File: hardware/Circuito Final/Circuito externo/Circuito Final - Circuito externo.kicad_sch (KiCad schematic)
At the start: 43 parts, among them J1 Conn_02x19_Odd_Even, J2 Conn_02x19_Odd_Even, J3 Conn_01x02, J4 Conn_01x02, Q1 FDMS6681Z, Q2 FDMS6681Z, Q3 MMBT2222A, SW1 SW_SPDT, SW2 SW_DIP_x04, SW3 SW_DIP_x04, SW4 SW_DIP_x01, SW5 SW_DIP_x01, SW6 SW_DIP_x01, U1 Opamp_Quad, U2 ICL7660, U3 INA180A1

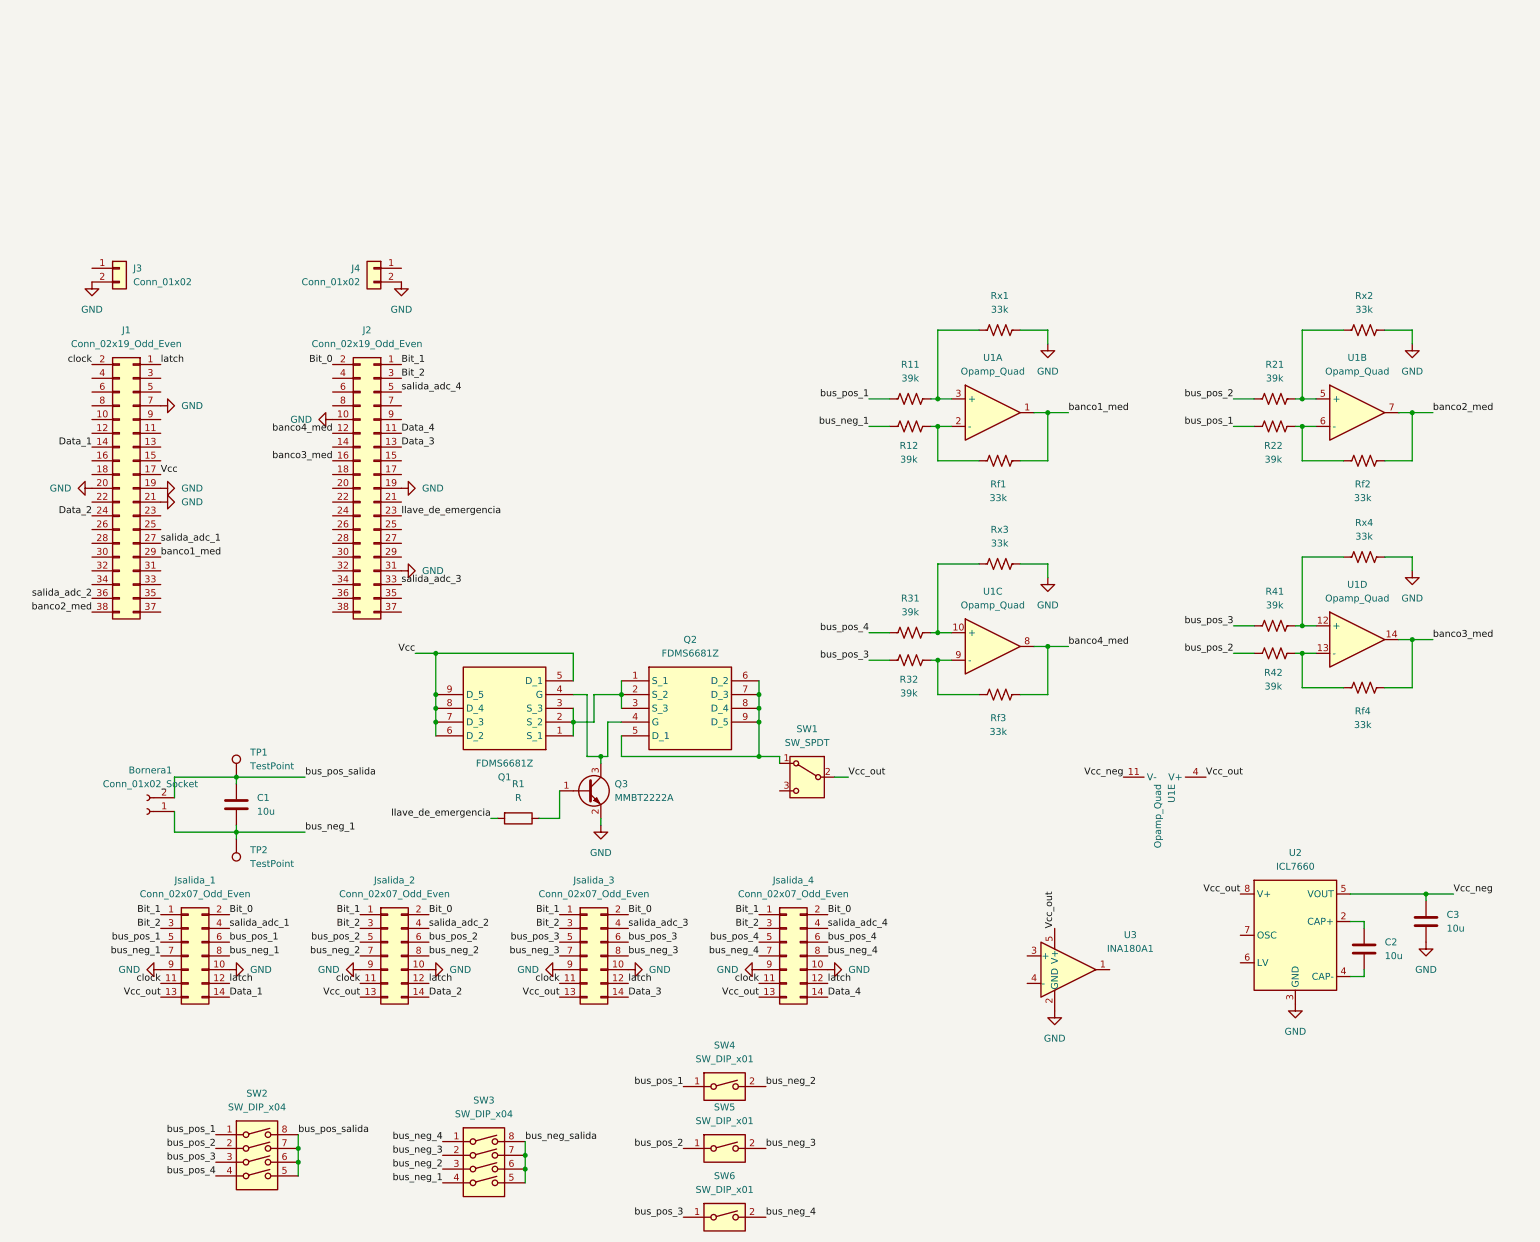
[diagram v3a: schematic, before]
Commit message: clasifica los bloques en el esquematico de kicad
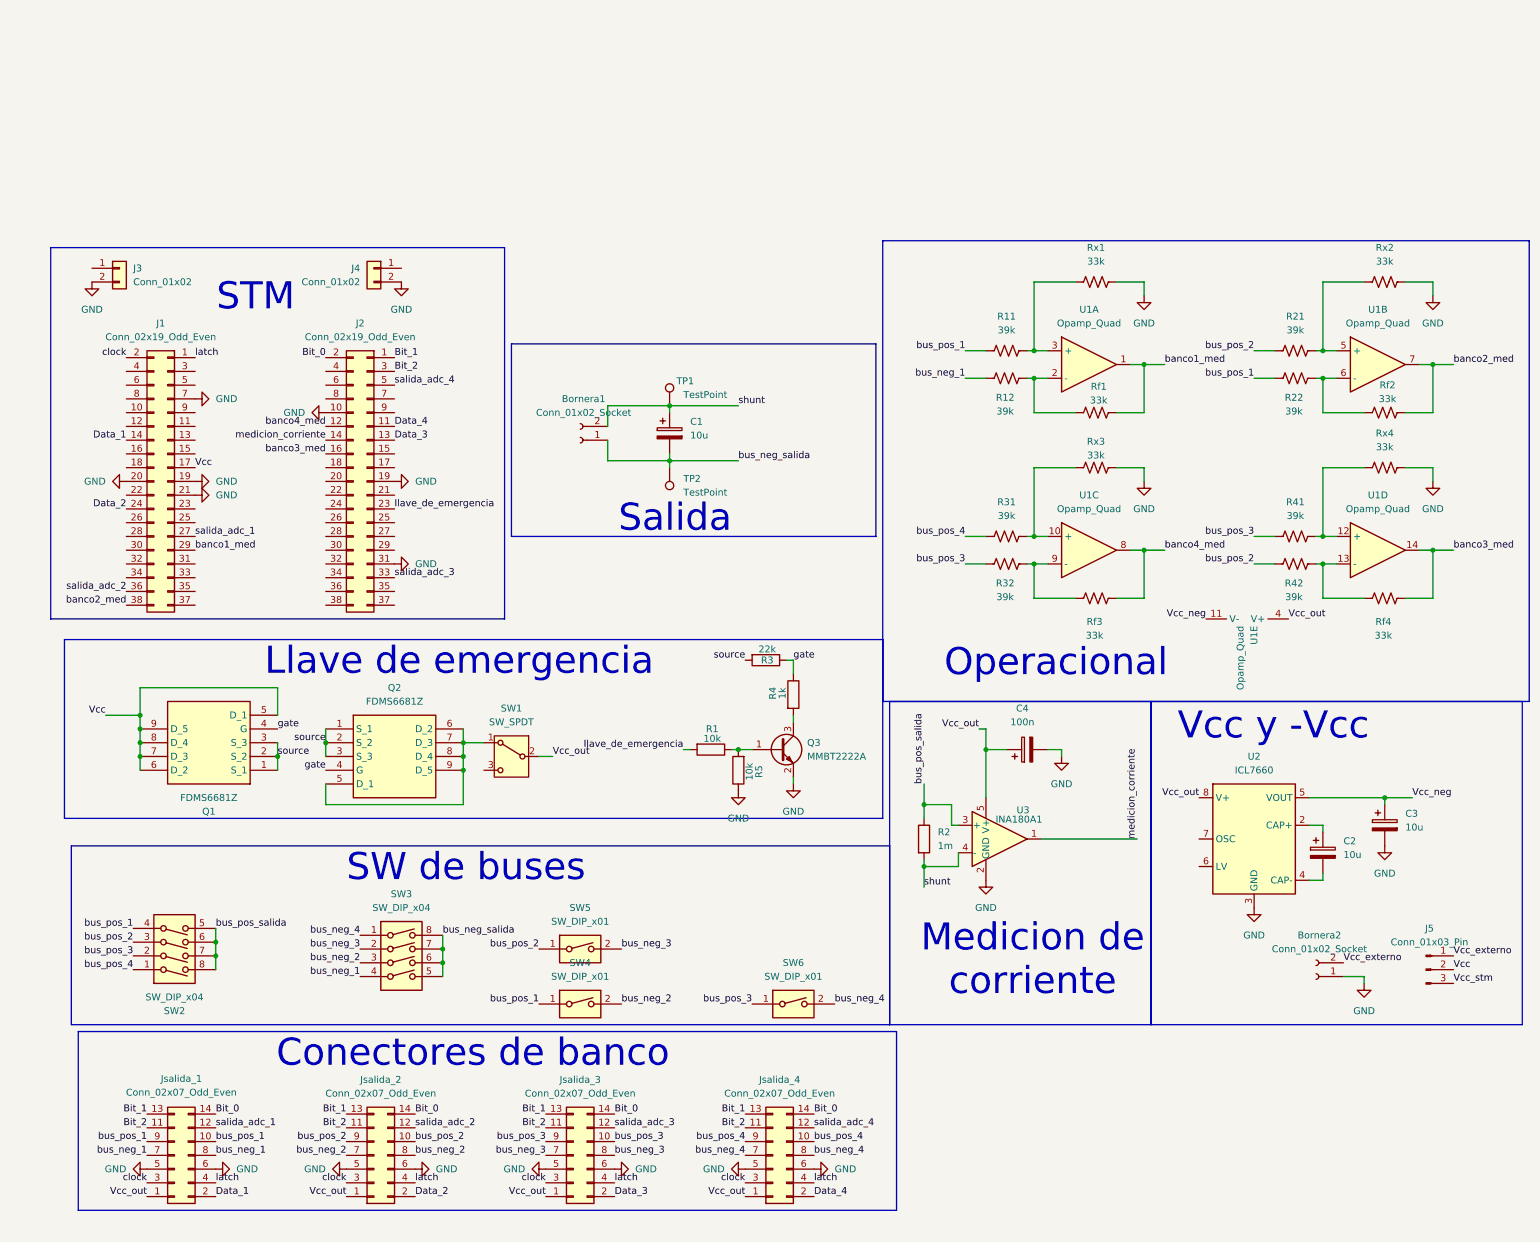
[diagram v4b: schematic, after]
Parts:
- added Bornera2: Conn_01x02_Socket, Huellas:TerminalBlock_bornier-2_P5.08mm, symbol Connector:Conn_01x02_Socket
- added C4: 100n, Capacitor_SMD:C_1206_3216Metric_Pad1.33x1.80mm_HandSolder, symbol Device:C_Polarized
- added J5: Conn_01x03_Pin, symbol Connector:Conn_01x03_Pin
- added R2: 1m, Resistor_SMD:R_2512_6332Metric_Pad1.40x3.35mm_HandSolder, symbol Device:R
- added R3: 22k, Resistor_SMD:R_1206_3216Metric_Pad1.30x1.75mm_HandSolder, symbol Device:R
- added R4: 1k, Resistor_SMD:R_1206_3216Metric_Pad1.30x1.75mm_HandSolder, symbol Device:R
- added R5: 10k, Resistor_SMD:R_1206_3216Metric_Pad1.30x1.75mm_HandSolder, symbol Device:R
- C1, C2, C3: symbol Device:C -> Device:C_Polarized
- Q1, Q2: footprint FDMS6681Z -> Huellas:FDMS6681Z
- R1: value R -> 10k; footprint (none) -> Resistor_SMD:R_1206_3216Metric_Pad1.30x1.75mm_HandSolder
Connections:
- net Bit_0: now also Jsalida_1.14 (Pin_14), Jsalida_2.14 (Pin_14), Jsalida_3.14 (Pin_14), Jsalida_4.14 (Pin_14); no longer Jsalida_1.2 (Pin_2), Jsalida_2.2 (Pin_2), Jsalida_3.2 (Pin_2), Jsalida_4.2 (Pin_2)
- net Bit_1: now also Jsalida_1.13 (Pin_13), Jsalida_2.13 (Pin_13), Jsalida_3.13 (Pin_13), Jsalida_4.13 (Pin_13); no longer Jsalida_1.1 (Pin_1), Jsalida_2.1 (Pin_1), Jsalida_3.1 (Pin_1), Jsalida_4.1 (Pin_1)
- net Bit_2: now also Jsalida_1.11 (Pin_11), Jsalida_2.11 (Pin_11), Jsalida_3.11 (Pin_11), Jsalida_4.11 (Pin_11); no longer Jsalida_1.3 (Pin_3), Jsalida_2.3 (Pin_3), Jsalida_3.3 (Pin_3), Jsalida_4.3 (Pin_3)
- net Data_1: now also Jsalida_1.2 (Pin_2); no longer Jsalida_1.14 (Pin_14)
- net Data_2: now also Jsalida_2.2 (Pin_2); no longer Jsalida_2.14 (Pin_14)
- net Data_3: now also Jsalida_3.2 (Pin_2); no longer Jsalida_3.14 (Pin_14)
- net Data_4: now also Jsalida_4.2 (Pin_2); no longer Jsalida_4.14 (Pin_14)
- net GND: now also Jsalida_1.5 (Pin_5), Jsalida_1.6 (Pin_6), Jsalida_2.5 (Pin_5), Jsalida_2.6 (Pin_6), Jsalida_3.5 (Pin_5), Jsalida_3.6 (Pin_6), Jsalida_4.5 (Pin_5), Jsalida_4.6 (Pin_6), Bornera2.1 (Pin_1), C4.2, R5.1; no longer Jsalida_1.10 (Pin_10), Jsalida_1.9 (Pin_9), Jsalida_2.10 (Pin_10), Jsalida_2.9 (Pin_9), Jsalida_3.10 (Pin_10), Jsalida_3.9 (Pin_9), Jsalida_4.10 (Pin_10), Jsalida_4.9 (Pin_9)
- net Vcc: now also J5.2 (Pin_2)
- net Vcc_out: now also Jsalida_1.1 (Pin_1), Jsalida_2.1 (Pin_1), Jsalida_3.1 (Pin_1), Jsalida_4.1 (Pin_1), C4.1; no longer Jsalida_1.13 (Pin_13), Jsalida_2.13 (Pin_13), Jsalida_3.13 (Pin_13), Jsalida_4.13 (Pin_13)
- net bus_neg_1: no longer Bornera1.1 (Pin_1), C1.2, TP2.1
- net bus_neg_salida: now also Bornera1.1 (Pin_1), C1.2, TP2.1
- net bus_pos_1: now also Jsalida_1.10 (Pin_10), Jsalida_1.9 (Pin_9), SW2.4; no longer Jsalida_1.5 (Pin_5), Jsalida_1.6 (Pin_6), SW2.1
- net bus_pos_2: now also Jsalida_2.10 (Pin_10), Jsalida_2.9 (Pin_9), SW2.3; no longer Jsalida_2.5 (Pin_5), Jsalida_2.6 (Pin_6), SW2.2
- net bus_pos_3: now also Jsalida_3.10 (Pin_10), Jsalida_3.9 (Pin_9), SW2.2; no longer Jsalida_3.5 (Pin_5), Jsalida_3.6 (Pin_6), SW2.3
- net bus_pos_4: now also Jsalida_4.10 (Pin_10), Jsalida_4.9 (Pin_9), SW2.1; no longer Jsalida_4.5 (Pin_5), Jsalida_4.6 (Pin_6), SW2.4
- net bus_pos_salida: now also U3.3 (+), R2.1; no longer Bornera1.2 (Pin_2), C1.1, TP1.1
- net clock: now also Jsalida_1.3 (Pin_3), Jsalida_2.3 (Pin_3), Jsalida_3.3 (Pin_3), Jsalida_4.3 (Pin_3); no longer Jsalida_1.11 (Pin_11), Jsalida_2.11 (Pin_11), Jsalida_3.11 (Pin_11), Jsalida_4.11 (Pin_11)
- net latch: now also Jsalida_1.4 (Pin_4), Jsalida_2.4 (Pin_4), Jsalida_3.4 (Pin_4), Jsalida_4.4 (Pin_4); no longer Jsalida_1.12 (Pin_12), Jsalida_2.12 (Pin_12), Jsalida_3.12 (Pin_12), Jsalida_4.12 (Pin_12)
- net salida_adc_1: now also Jsalida_1.12 (Pin_12); no longer Jsalida_1.4 (Pin_4)
- net salida_adc_2: now also Jsalida_2.12 (Pin_12); no longer Jsalida_2.4 (Pin_4)
- net salida_adc_3: now also Jsalida_3.12 (Pin_12); no longer Jsalida_3.4 (Pin_4)
- net salida_adc_4: now also Jsalida_4.12 (Pin_12); no longer Jsalida_4.4 (Pin_4)
- net medicion_corriente: now reaches J2.14 (Pin_14)
- net medicion_corriente: now also U3.1
- net at Q3.1 (B), R1.1: now also R5.2
- net gate: now reaches Q1.4 (G), Q2.4 (G)
- net gate: now also R3.1, R4.1; no longer Q3.3 (C)
- net source: now reaches Q1.1 (S_1), Q1.2 (S_2), Q1.3 (S_3), Q2.1 (S_1), Q2.2 (S_2), Q2.3 (S_3)
- net source: now also R3.2
- net shunt: now reaches U3.4 (-)
- net shunt: now also Bornera1.2 (Pin_2), C1.1, TP1.1, R2.2
- new net: Q3.3 (C), R4.2
- new net Vcc_externo: Bornera2.2 (Pin_2), J5.1 (Pin_1)
- new net Vcc_stm: J5.3 (Pin_3)
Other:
- note added: "Conectores de banco"
- note added: "Llave de emergencia"
- note added: "Medicion de corriente"
- note added: "Operacional"
- note added: "STM"
- note added: "SW de buses"
- note added: "Salida"
- note added: "Vcc y -Vcc"
- moved on the sheet: Bornera1, J1, J2, Q1, Q2, Q3, R1, R11, R12, R21, R22, R31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

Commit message: conexiones de los integrados y sus resistencias
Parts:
- removed C4: 100n, Capacitor_SMD:C_1206_3216Metric_Pad1.33x1.80mm_HandSolder, symbol Device:C_Polarized
- added C5, C6, C7, C8: 100n, Capacitor_SMD:C_1206_3216Metric_Pad1.33x1.80mm_HandSolder, symbol Device:C_Small
- J5: footprint (none) -> Connector_PinHeader_1.27mm:PinHeader_1x03_P1.27mm_Vertical
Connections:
- net GND: now also C3.1, C5.1, C6.1, C7.1, C8.1; no longer C3.2
- net Vcc: no longer J1.17 (Pin_17)
- net Vcc_neg: now also C3.2, C7.2; no longer C3.1
- net Vcc_out: now also C5.2, C6.2, C8.2
- net Vcc_stm: now also J1.15 (Pin_15)
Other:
- moved on the sheet: C2, C3, SW1, U2

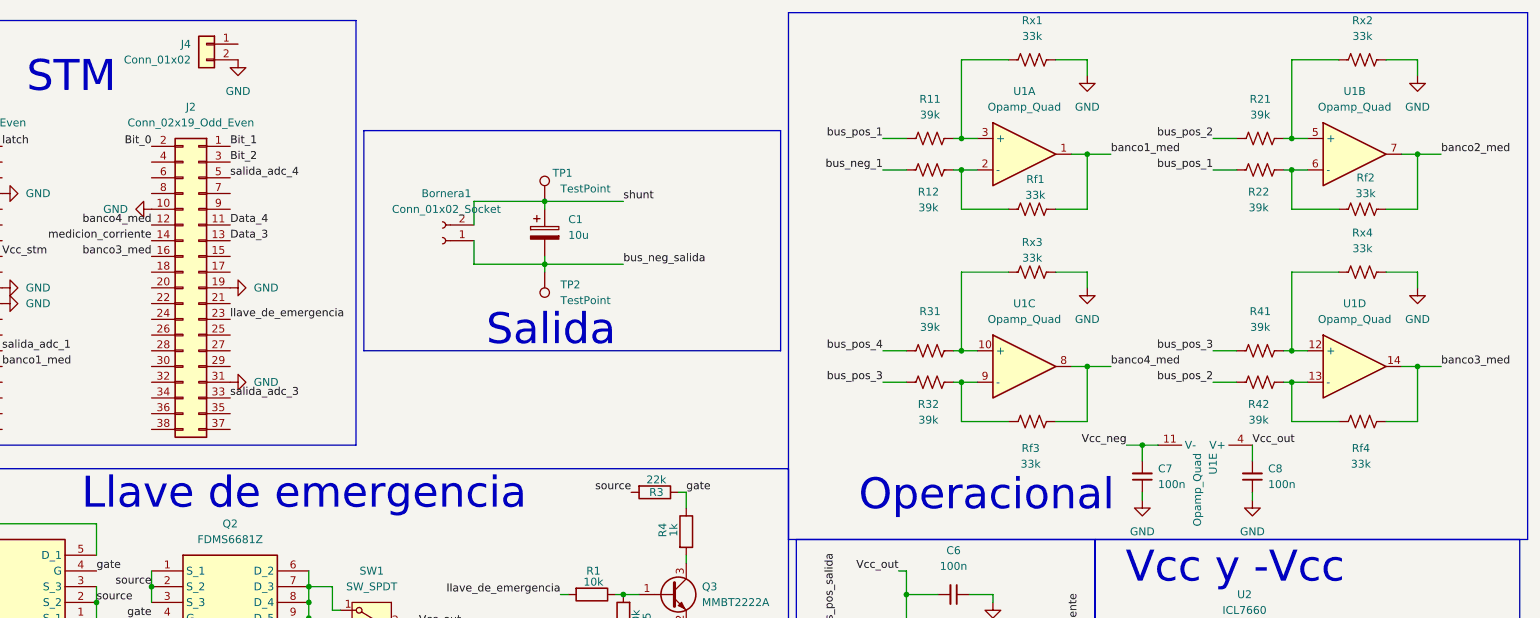
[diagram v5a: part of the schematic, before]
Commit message: conectores de banco ruteados
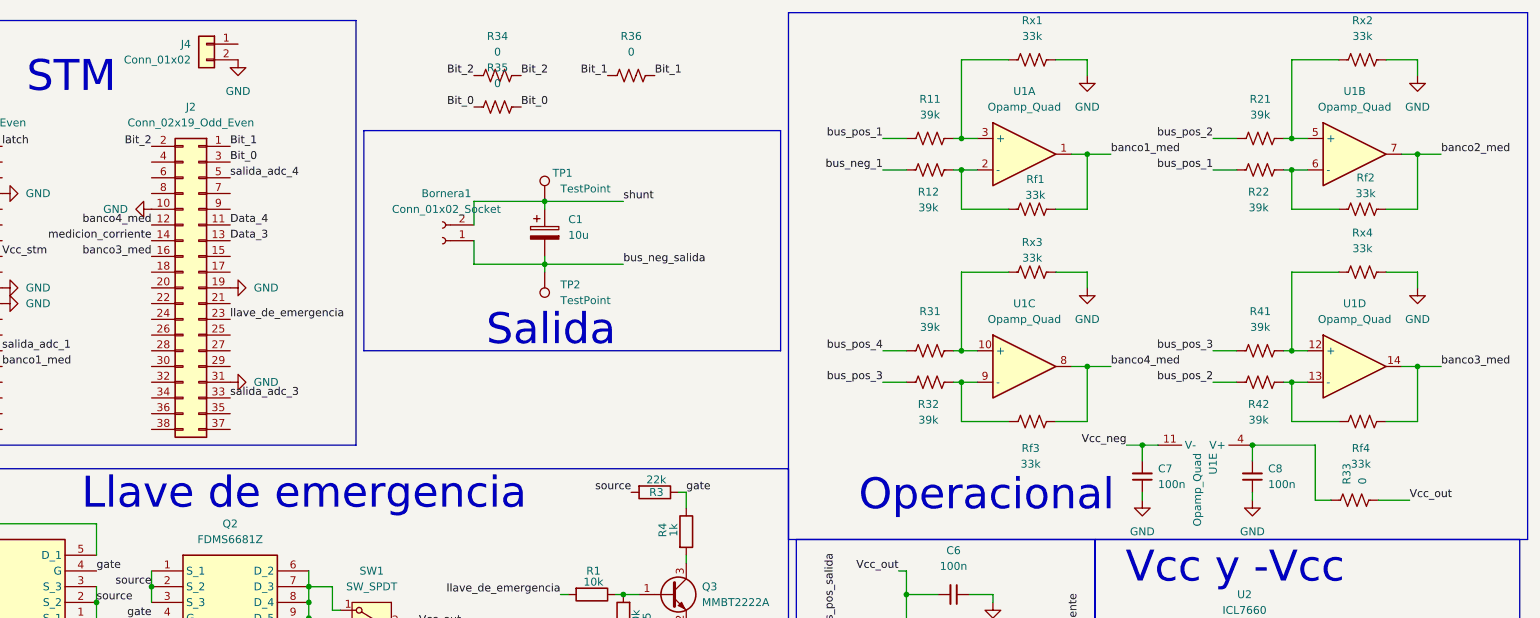
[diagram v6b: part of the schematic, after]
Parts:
- added R33, R34, R35, R36: 0, Resistor_SMD:R_1206_3216Metric_Pad1.30x1.75mm_HandSolder, symbol Device:R_US
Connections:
- net Bit_0: now also J2.3 (Pin_3), R35.1, R35.2; no longer J2.2 (Pin_2)
- net Bit_1: now also R36.1, R36.2
- net Bit_2: now also J2.2 (Pin_2), R34.1, R34.2; no longer J2.3 (Pin_3)
- net Vcc_out: now also R33.1; no longer C8.2, U1.4 (V+)
- new net: C8.2, R33.2, U1.4 (V+)

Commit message: ya esta todo conectado, spoiler: un quilombo
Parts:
- added R37, R38, R39, R40, R43, R44, R45, R46, R47, R48: 0, Resistor_SMD:R_1206_3216Metric_Pad1.30x1.75mm_HandSolder, symbol Device:R_US
- J5: footprint Connector_PinHeader_1.27mm:PinHeader_1x03_P1.27mm_Vertical -> Connector_PinHeader_2.54mm:PinHeader_1x03_P2.54mm_Vertical
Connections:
- net Bit_0: no longer R35.1, R35.2
- net GND: now also R45.1, R45.2, R46.1, R46.2, R47.1, R47.2
- net Vcc: now also R39.1, R39.2, R40.1, R40.2
- net Vcc_out: now also R43.1, R43.2, R48.1, R48.2
- net Vcc_stm: now also R38.1, R38.2
- net bus_neg_1: now also R44.1, R44.2
- net latch: now also R35.1, R35.2, R37.1, R37.2
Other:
- moved on the sheet: R34, R35, R36
